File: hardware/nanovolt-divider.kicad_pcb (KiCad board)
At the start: 2 copper layers, 60 x 94 mm, 75 parts, among them J1 NORMAL IN +, J2 NORMAL IN -, J3 HV IN +, J5 DIVIDER OUT HI, J6 DIVIDER OUT LO, J7 ESP32_DISP_P1, J8 ESP32_DISP_CN1, J9 ESP32_DISP_P3, K1 TQ2-L2-5V, K2 TQ2-L2-5V, K3 TQ2-L2-5V, K4 TQ2-L2-5V, K5 TQ2-L2-5V, Q1 MMBT2222A, Q10 MMBT2222A, Q2 MMBT2222A, Q3 MMBT2222A, Q4 MMBT2222A, Q5 MMBT2222A, Q6 MMBT2222A, Q7 MMBT2222A, Q8 MMBT2222A, Q9 MMBT2222A, SW1 SW_3PDT NORMAL/HV, U1 MCP23017-E/SO, U2 TMP275AIDR

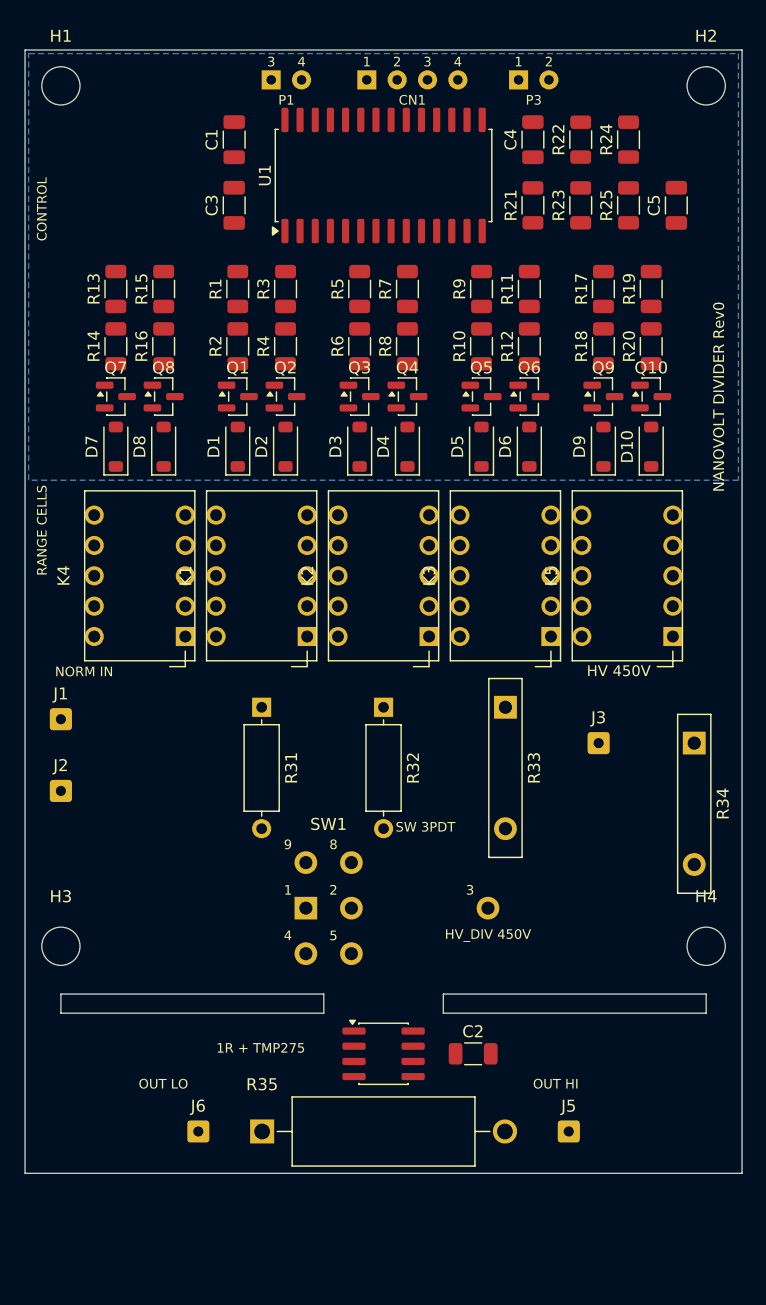
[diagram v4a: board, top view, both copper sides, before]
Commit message: Remove the 450 V path: keep the instrument single-purpose
The HV input shared the 1 ohm low leg, and that shared leg capped what the
range could ever be. At 10 M the divider drew 45 uA and gave 45 uV out;
more output meant a smaller high leg, and 1 M draws 450 uA where 10 M
draws 45 uA. A Geiger supply is built to source microamps into a tube that
draws almost none, so its output impedance is high - often set by a series
anode resistor. Against a 1 M source impedance a 10 M divider already
reads 9% low and a 1 M divider reads 50% low, and that error tracks the
supply's operating point, so calibration cannot remove it.

The HV path also had no polarity reversal - K4 serves the NORMAL input
only - so thermal EMF and DMM offset could not be nulled by ABBA the way
they are on the normal ranges. More output was exactly what that path
needed, and the shared 1 ohm leg was the one thing that would not give it.

A dedicated fixed divider has none of those constraints because it picks
its own low leg, so the 450 V measurement moves out of this instrument.

SW1's two analog poles were only ever selecting between the normal path
and the HV path, so with the HV path gone both collapse to plain nets:
K5 A_NO lands directly on MEAS_NODE and B_NO directly on ANALOG_RTN.
ISOLATE is untouched - K5 was always what performed it.

Removed: R34, J3, SW1 and the panel toggle, R24/R25/C5, the J9/P3
harness, the SW_3PDT symbol and its wire-pad footprint, the J_ESP32_P3
symbol and footprint, the HV netclass (generator template and the live
.kicad_pro), and all three HV rules from .kicad_dru - which is now down to
the single bridge-track-width rule. 71 components to 64. The panel is four
banana jacks with nothing wired panel-to-panel, so every conductor now
appears in the netlist.

Board 60 x 94 -> 60 x 83. Getting the full 11 mm needed one extra move:
J1/J2 sat below the relay row, directly above the lower-left mounting
hole, which pinned that hole and through it the slots and the whole 1 oh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
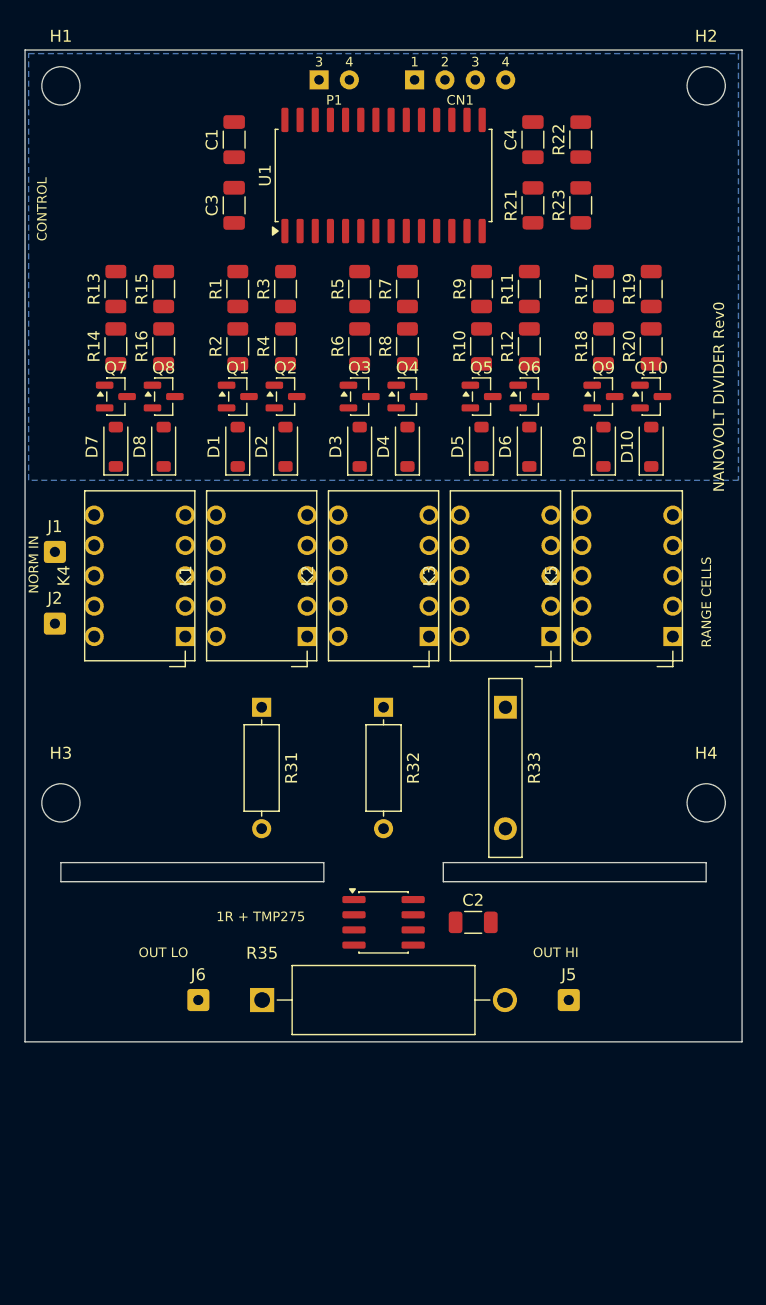
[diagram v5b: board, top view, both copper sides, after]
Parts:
- removed C5: 10n, Capacitor_SMD:C_1206_3216Metric
- removed J3: HV IN +, Connector_Wire:SolderWire-0.25sqmm_1x01_D0.65mm_OD1.7mm
- removed J9: ESP32_DISP_P3, nanovolt-divider:J_ESP32_P3_WirePads
- removed R24: 10k, Resistor_SMD:R_1206_3216Metric
- removed R25: 100k, Resistor_SMD:R_1206_3216Metric
- removed R34: 10M, nanovolt-divider:R_Radial_Ohmite_SlimMox_SM102_L14.7mm_W2.5mm_P10.16mm
- removed SW1: SW_3PDT NORMAL/HV, nanovolt-divider:SW_3PDT_WirePads_Split
- moved J1 14.0 mm to (52.5, 92.0)
- moved J2 14.0 mm to (52.5, 98.0)
- moved H3 12.0 mm to (53.0, 113.0)
- moved H4 12.0 mm to (107.0, 113.0)
- moved C2 11.0 mm to (87.5, 123.0)
- moved J5 11.0 mm to (95.5, 129.5)
- moved J6 11.0 mm to (64.5, 129.5)
- moved R35 11.0 mm to (69.8, 129.5)
- moved U2 11.0 mm to (80.0, 123.0)
- moved J7 4.00 mm to (74.6, 52.5)
- moved J8 4.00 mm to (82.6, 52.5)
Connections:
- K5 pad 4: /INJ_NODE -> /MEAS_NODE
- K5 pad 7: /INJ_RTN -> /ANALOG_RTN
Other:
- board size 60 x 94 mm -> 60 x 83 mm
- board text removed: "HV 450V"
- board text removed: "SW 3PDT"

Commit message: Lay the high legs flat and go to M2: board 60 x 83 -> 60 x 72.5
Two independent constraints were holding the board down, and both were mine
rather than the design's.

R31-R33 standing vertically under their relays were 16 mm tall, and R33
reached y 67.7 with the slots at 68.0 - 0.31 mm of margin. The mounting
holes, which I had assumed were binding, had 1.55 mm. Flat they are 3.2 mm
tall and the row clears the relays by 0.55 mm: 9 mm off the board.

They no longer align one per relay, because they cannot - three 12 mm-plus
resistors do not fit in three 10.2 mm relay cells. Nothing is lost by that.
A_NO and B_NO are both on the relay's *upper* contact row, so a resistor
hanging below the relay never landed across them either; it ran 14 mm to one
and 24 mm to the other. Flat and offset, both runs are 2-5 mm. Rotation 180
keeps pad 1 (R*_IN, from A_NO) on A_NO's side of the relay.

M2 mounting holes instead of M3 for the remaining 1.5 mm. The hole is only
1 mm smaller but the courtyard radius drops 3.45 -> 2.45, and both ends of
that count: the top sets how close the hole sits under K4/K5, the bottom sets
how close the slots sit under the hole. The lower pair now sits in the same
band as the high-leg row, flanking it at the board edges. The M2 footprint
puts its designator 3.15 mm above the hole rather than 4.15, which landed
H1/H2's refdes across the top board edge - all four move to F.Fab, which
they should have been anyway as board_only parts excluded from the BOM and
the pick-and-place.

ERC 0 violations, 0 schematic-parity issues. DRC 64 violations, and the
violation set is byte-identical to the previous board - all silk-over-copper,
the class parked until after routing.

Co-Authored-By: Claude Opus 5 <noreply@anthropic.com>
Claude-Session: https://claude.ai/code/session_01U9ZxpmaweJaWAXeWHjtGtX
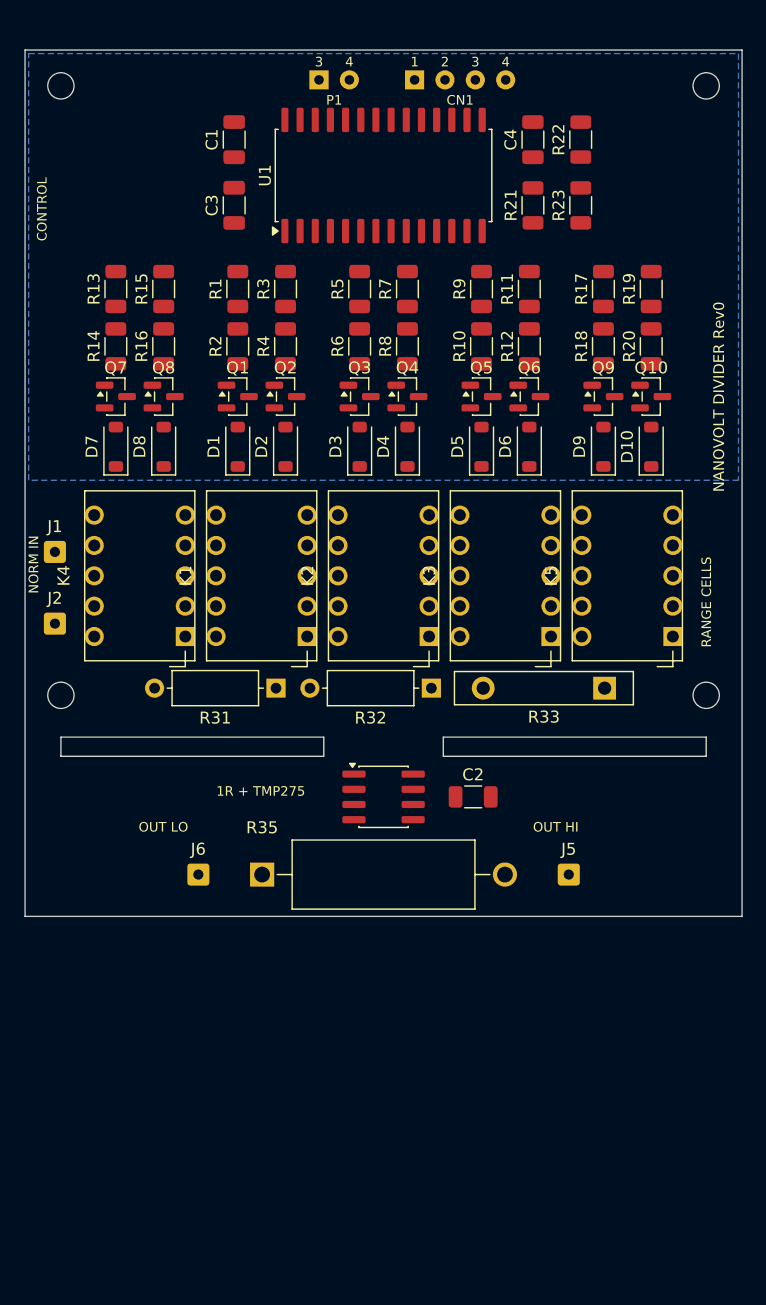
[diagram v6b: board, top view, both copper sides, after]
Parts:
- H1, H2, H3, H4: value M3 -> M2; footprint MountingHole:MountingHole_3.2mm_M3 -> MountingHole:MountingHole_2.2mm_M2
- moved C2 10.5 mm to (87.5, 112.5)
- moved J5 10.5 mm to (95.5, 119.0)
- moved J6 10.5 mm to (64.5, 119.0)
- moved R35 10.5 mm to (69.8, 119.0)
- moved U2 10.5 mm to (80.0, 112.5)
- moved H3 9.00 mm to (53.0, 104.0)
- moved H4 9.00 mm to (107.0, 104.0)
- moved R33 8.45 mm to (98.5, 103.4), turned to 180 degrees
- moved R32 4.31 mm to (84.0, 103.4), turned to 180 degrees
- moved R31 2.00 mm to (71.0, 103.4), turned to 180 degrees
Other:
- board size 60 x 83 mm -> 60 x 72.5 mm

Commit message: Fold the harness pads into the MCP23017 row: board 60 x 72.5 -> 60 x 69.1
The display-module pads had a row of their own above U1, but they are only
2.9 mm tall against U1's 11.9 - beside it rather than above it they cost no
height at all. The control band is now one row:

  [H1] P1/CN1 | C1,C3 | U1 | C4,R21 | R22,R23 [H2]

P1 is stacked above CN1 rather than beside it. Side by side the two groups
are 17.2 mm wide and the band needs 48.2 mm of the 49.1 mm between the top
mounting holes, which does not fit - the right-hand columns' designators
overlapped their neighbours. Stacked the block is 11.1 mm wide and 7.7 mm
tall, still inside U1's band, so the width comes free. P1 and CN1 are
separate 4-pin connectors on the module and therefore separate pigtails, so
one landing above the other crosses nothing.

Worth recording because it was not obvious: what sets the column gaps is each
column's *designator*, which sits 1.85 mm to its left, not the parts. Packing
by part width alone puts the refdes of every column on top of its neighbour.

ERC 0 violations, 0 schematic-parity issues. DRC 64 violations, violation set
byte-identical to the previous board.

Co-Authored-By: Claude Opus 5 <noreply@anthropic.com>
Claude-Session: https://claude.ai/code/session_01U9ZxpmaweJaWAXeWHjtGtX
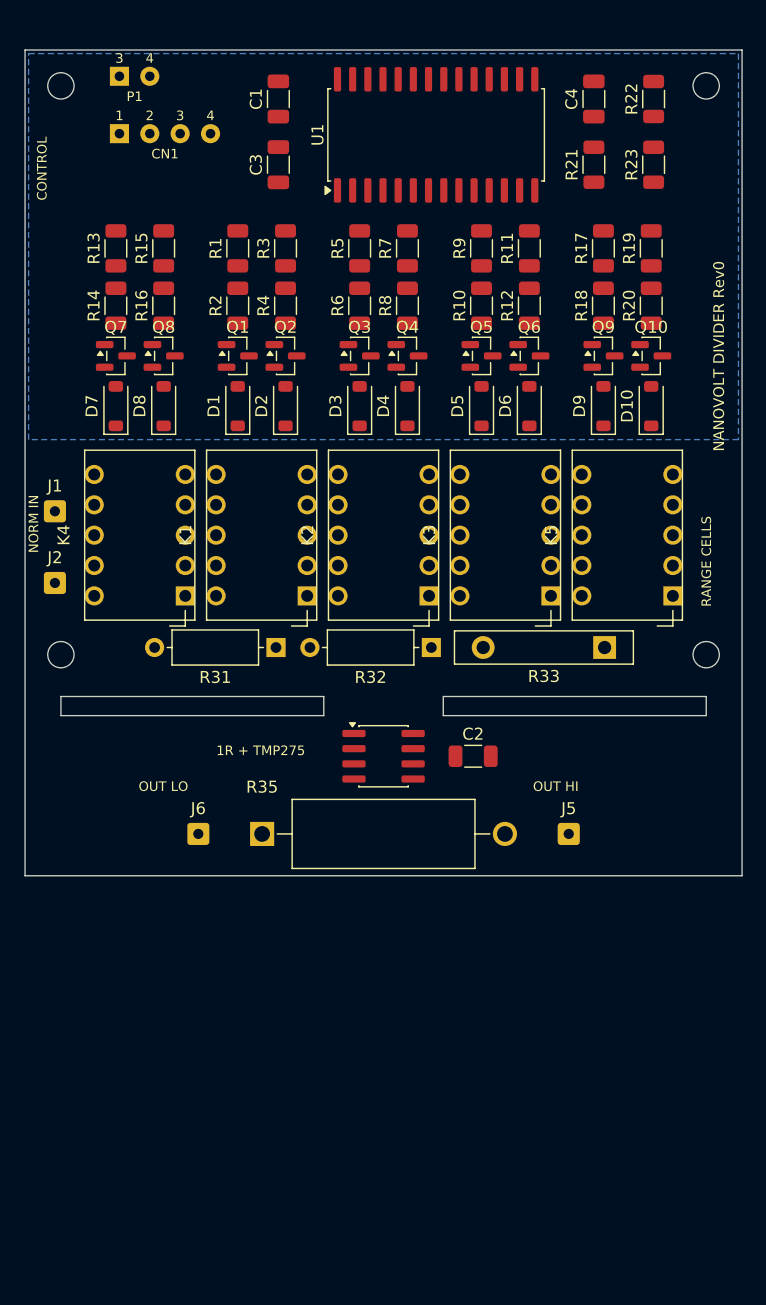
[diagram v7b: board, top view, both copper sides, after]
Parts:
- moved J8 25.1 mm to (57.9, 57.0)
- moved J7 16.7 mm to (57.9, 52.2)
- moved R22 6.98 mm to (102.6, 54.1)
- moved R23 6.98 mm to (102.6, 59.6)
- moved C4 6.13 mm to (97.6, 54.1)
- moved R21 6.13 mm to (97.6, 59.6)
- moved U1 5.56 mm to (84.4, 57.1)
- moved C1 5.02 mm to (71.2, 54.1)
- moved C3 5.02 mm to (71.2, 59.6)
- moved C2 3.40 mm to (87.5, 109.1)
- moved D1 3.40 mm to (67.8, 79.8)
- moved D10 3.40 mm to (102.4, 79.8)
- moved D2 3.40 mm to (71.8, 79.8)
- moved D3 3.40 mm to (78.0, 79.8)
- moved D4 3.40 mm to (82.0, 79.8)
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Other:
- board size 60 x 72.5 mm -> 60 x 69.1 mm

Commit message: Place the control-band passives by net rather than by what fit
U1's VDD(9), VSS(10), SCL(12) and SDA(13) are all on its lower pad row at
x 36.3-41.4 and ~RESET(18) on the upper row, while power and I2C both arrive
at the harness on the far left. The three passive columns now follow that:

  L1, at the power entry : C3 22u 5 V bulk, C4 22u 3V3 bulk
  L2, adjacent to U1     : R21 SDA and R22 SCL pull-ups
  R1, right of U1        : R23 ~RESET pull-up (upper, level with pin 18)
                           C1 100n across VDD/VSS (lower, level with 9/10)

The pull-ups were on the far side of U1, which made the I2C bus run out past
pin 13 and back. Between CN1 and U1 it is monotonic. Measured pad to pad:

  SCL bus   56.1 -> 35.3 mm   (and no longer doubles back)
  SDA bus   41.1 -> 34.5 mm   (likewise)
  C4 -> 3V3 entry  32.1 -> 7.2 mm
  R23 -> ~RESET    16.2 -> 9.2 mm
  C1 -> VDD        16.3 -> 11.2 mm
  C3 -> 5 V entry  16.0 -> 13.9 mm

C1 is right of U1 rather than left because U1 sits at x 39.5 with its power
pins mid-row: 10.0 mm from R1 against 13.8 mm from L2. 10 mm is further than
a decoupler should be, but U1 is 18.4 mm wide with those pins in the middle
and the band has no room below it, so it is the best slot on offer - on a
static 3.3 V rail drawing about 1 mA.

Board size unchanged at 60 x 69.1. ERC 0 violations, 0 schematic-parity
issues, DRC 64 violations with the set byte-identical to the previous board.

Co-Authored-By: Claude Opus 5 <noreply@anthropic.com>
Claude-Session: https://claude.ai/code/session_01U9ZxpmaweJaWAXeWHjtGtX
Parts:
- moved C1 31.9 mm to (102.6, 59.6)
- moved C4 26.8 mm to (71.4, 59.6)
- moved R22 26.7 mm to (76.5, 59.6)
- moved R21 21.8 mm to (76.5, 54.1)
- moved C3 5.50 mm to (71.4, 54.1)
- moved R23 5.50 mm to (102.6, 54.1)
- moved U1 5.10 mm to (89.5, 57.1)
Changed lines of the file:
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@@
 	(footprint "Resistor_SMD:R_1206_3216Metric"
 		(layer "F.Cu")
-		(at 102.6 59.6 90)
+		(at 102.6 54.1 90)
 		(descr "Resistor SMD 1206 (3216 Metric), square (rectangular) end terminal, IPC-7351 nominal, (Body size source: IPC-SM-782 page 72, https://www.pcb-3d.com/wordpress/wp-content/uploads/ipc-sm-782a_amendment_1_and_2.pdf)")
 		(tags "resistor")
@@
 	(footprint "Resistor_SMD:R_1206_3216Metric"
 		(layer "F.Cu")
-		(at 97.6 59.6 90)
+		(at 76.5 54.1 90)
 		(descr "Resistor SMD 1206 (3216 Metric), square (rectangular) end terminal, IPC-7351 nominal, (Body size source: IPC-SM-782 page 72, https://www.pcb-3d.com/wordpress/wp-content/uploads/ipc-sm-782a_amendment_1_and_2.pdf)")
 		(tags "resistor")
@@
 	(footprint "Capacitor_SMD:C_1206_3216Metric"
 		(layer "F.Cu")
-		(at 71.2 59.6 90)
+		(at 71.4 54.1 90)
 		(descr "Capacitor SMD 1206 (3216 Metric), square (rectangular) end terminal, IPC-7351 nominal, (Body size source: IPC-SM-782 page 76, https://www.pcb-3d.com/wordpress/wp-content/uploads/ipc-sm-782a_amendment_1_and_2.pdf)")
 		(tags "capacitor")
@@
 	(footprint "Capacitor_SMD:C_1206_3216Metric"
 		(layer "F.Cu")
-		(at 97.6 54.1 90)
+		(at 71.4 59.6 90)
 		(descr "Capacitor SMD 1206 (3216 Metric), square (rectangular) end terminal, IPC-7351 nominal, (Body size source: IPC-SM-782 page 76, https://www.pcb-3d.com/wordpress/wp-content/uploads/ipc-sm-782a_amendment_1_and_2.pdf)")
 		(tags "capacitor")
@@
 	(footprint "Capacitor_SMD:C_1206_3216Metric"
 		(layer "F.Cu")
-		(at 71.2 54.1 90)
+		(at 102.6 59.6 90)
 		(descr "Capacitor SMD 1206 (3216 Metric), square (rectangular) end terminal, IPC-7351 nominal, (Body size source: IPC-SM-782 page 76, https://www.pcb-3d.com/wordpress/wp-content/uploads/ipc-sm-782a_amendment_1_and_2.pdf)")
 		(tags "capacitor")
@@
 	(footprint "Package_SO:SOIC-28W_7.5x17.9mm_P1.27mm"
 		(layer "F.Cu")
-		(at 84.4 57.1 90)
+		(at 89.5 57.1 90)
 		(descr "SOIC, 28 Pin (JEDEC MS-013AE, https://www.analog.com/media/en/package-pcb-resources/package/35833120341221rw_28.pdf)")
 		(tags "SOIC SO")
@@
 	(footprint "Resistor_SMD:R_1206_3216Metric"
 		(layer "F.Cu")
-		(at 102.6 54.1 90)
+		(at 76.5 59.6 90)
 		(descr "Resistor SMD 1206 (3216 Metric), square (rectangular) end terminal, IPC-7351 nominal, (Body size source: IPC-SM-782 page 72, https://www.pcb-3d.com/wordpress/wp-content/uploads/ipc-sm-782a_amendment_1_and_2.pdf)")
 		(tags "resistor")
